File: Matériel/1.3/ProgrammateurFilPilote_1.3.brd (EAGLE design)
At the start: 85.1 x 66.7 mm, 84 parts, among them IC1 MCP23017, J2 GROVE-I2C, P1 PADSMALL, P2 PADSMALL, SW1 HLS8L-DC5V-S-C, T1 2N3904, T2 BSS138

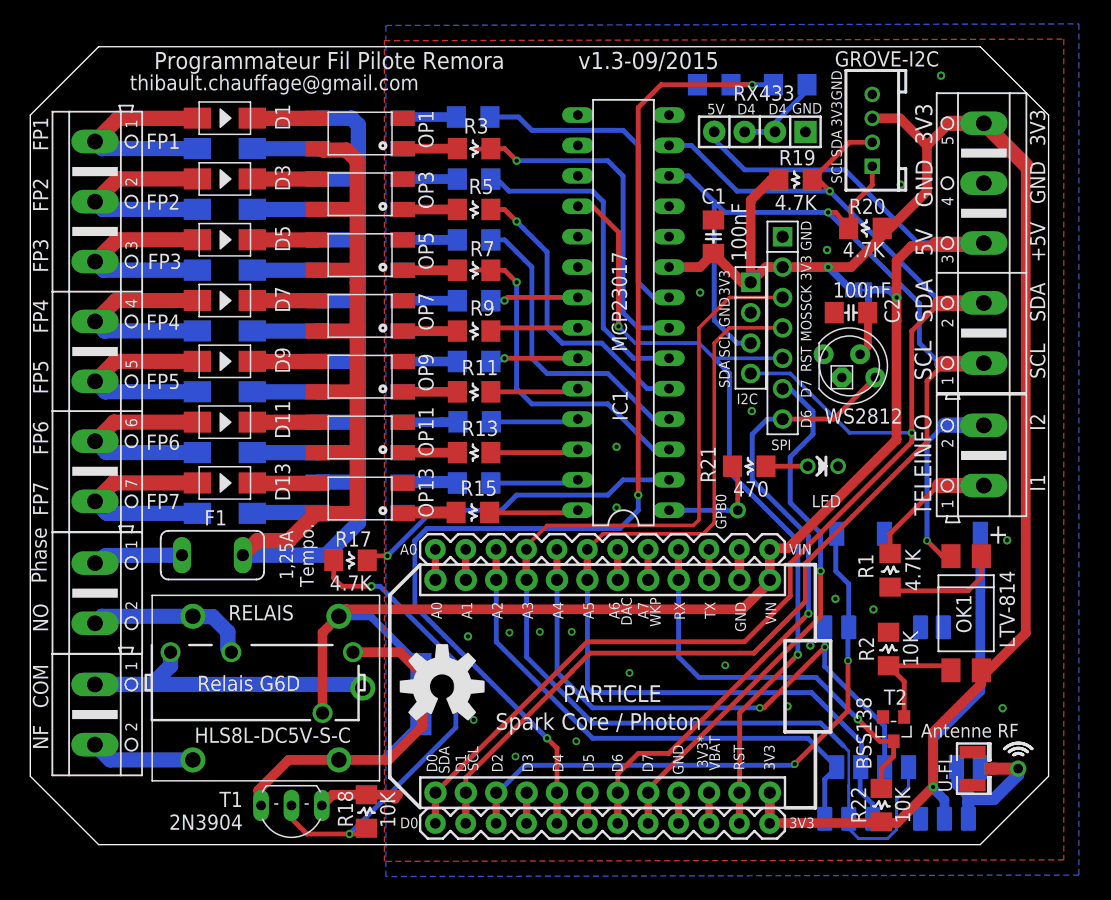
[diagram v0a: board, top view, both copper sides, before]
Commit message: Ajustements Finaux
Résistances 390 Ohm pour nouveaux optos Sharp
Commandes Opto/led via MCP par la masse
Ajustement des borniers pour boitier rail DIN
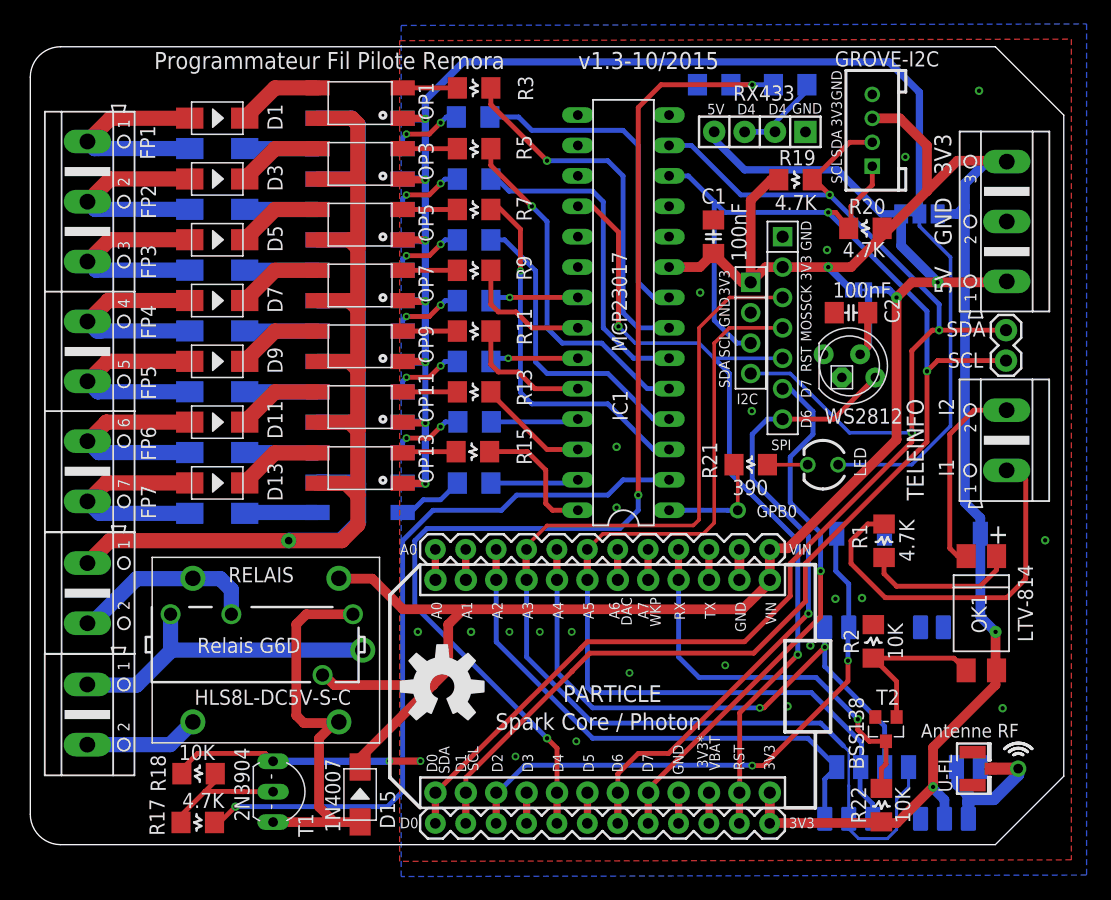
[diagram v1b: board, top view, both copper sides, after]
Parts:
- removed EXTENSION: (no value), con-ptr500:AK500/5
- removed F1: 1,25A temporisé, fuse:TE5
- added JP1: (no value), SparkFun-Connectors:1X02
- added OPTO: (no value), SparkFun-Passives:PAD-JUMPER-3-2OF3_NC_BY_TRACE_YES_SILK_LARGE
- added X1: (no value), con-ptr500:AK500/3
- LED: value (none) -> LED3MM; device _c2h:LED3MM_NOSILK -> _c2h:LED3MM
- R10, R11, R12, R13, R14, R15, R16, R21, R3, R4, R5, R6, R7, R8, R9: value 470 -> 390
- moved R17 25.4 mm to (14.0, 1.86)
- moved R18 14.4 mm to (14.1, 5.93), turned to 0 degrees
- moved D15 9.80 mm to (27.6, 4.19), flipped to the top
- moved R7 5.08 mm to (37.1, 53.1)
- moved R15 5.08 mm to (37.0, 32.8)
- moved R11 5.08 mm to (37.1, 42.9)
- moved R13 5.08 mm to (37.1, 37.8)
- moved R3 5.08 mm to (37.1, 63.2)
- moved R5 5.08 mm to (37.1, 58.2)
- moved R9 5.08 mm to (37.1, 48.0)
- moved RELAIS 3.18 mm to (18.9, 16.8)
- moved SW1 3.18 mm to (19.7, 16.3)
- moved OP5 2.54 mm to (30.7, 53.1)
- moved OP1 2.54 mm to (30.7, 63.2)
- moved OP11 2.54 mm to (30.7, 37.8)
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- renumbered SJ1 to RGB
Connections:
- removed net PHASE-SECTEUR: 230V.1, F1.1
- new net N$18: OP9.3, R11.2
- net +3V3: now also OPTO.1, X1.3; no longer EXTENSION.5
- net +5V: now also OPTO.3, X1.1; no longer EXTENSION.3
- net GND: now also X1.2; no longer EXTENSION.4, LED.MINUS, OP1.3, OP10.3, OP11.3, OP12.3, OP13.3, OP14.3, OP2.3, OP3.3, OP4.3, OP5.3, OP6.3, OP7.3, OP8.3, OP9.3
- net LED: now also R21.1; no longer R21.2
- net N$10: now also OP4.3; no longer OP4.1
- net N$11: now also OP5.3; no longer OP5.1
- net N$12: now also OP6.3; no longer OP6.1
- net N$13: now also OP7.3; no longer OP7.1
- net N$14: now also OP8.3; no longer OP8.1
- net N$19: now also LED.PLUS, OP1.1, OP10.1, OP11.1, OP12.1, OP13.1, OP14.1, OP2.1, OP3.1, OP4.1, OP5.1, OP6.1, OP7.1, OP8.1, OPTO.2; no longer R11.2
- net N$32: now also OP10.3; no longer OP10.1
- net N$34: now also OP14.3; no longer OP14.1
- net N$47: now also OP11.3; no longer OP11.1
- net N$48: now also OP12.3; no longer OP12.1
- net N$6: now also LED.MINUS, R21.2; no longer LED.PLUS, R21.1
- net N$7: now also OP1.3; no longer OP1.1
- net N$8: now also OP2.3; no longer OP2.1
- net N$9: now also OP3.3; no longer OP3.1
- net PHASE: now also 230V.1; no longer F1.2
- net S$5: now also OP13.3; no longer OP13.1
- net SCL: now also JP1.2; no longer EXTENSION.1
- net SDA: now also JP1.1; no longer EXTENSION.2
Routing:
- net N$19: track 4.57 -> 143.4 mm, vias 0 -> 7
- net RELAIS: track 29.0 -> 62.1 mm
- net N$21: track 41.1 -> 12.5 mm, vias 2 -> 0
- net N$5: track 11.2 -> 31.9 mm
- net +3V3: track 159.2 -> 138.9 mm, vias 2 -> 3
- net PHASE: track 131.2 -> 147.6 mm, vias 0 -> 1
- net GND: track 13.4 -> 26.3 mm, vias 22 -> 24
- net +5V: track 123.9 -> 131.7 mm, vias 1 -> 2
- net PHASE-SECTEUR: track 7.47 -> 0.00 mm
- net SCL: track 126.9 -> 122.1 mm, vias 1 -> 2
- net SDA: track 131.1 -> 126.5 mm, vias 2 -> 3
- net N$18: track 0.00 -> 4.57 mm
- net FP2A: track 24.8 -> 29.2 mm
- net FP3A: track 27.5 -> 31.4 mm
- net FP7A: track 7.44 -> 11.0 mm
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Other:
- board size 85.1 x 66.7 mm -> 86.4 x 66.7 mm
- board text added: "v1.3-10/2015"
- board text removed: "1,25A Tempo."
- board text removed: "Fusible"
- board text removed: "thibault.chauffage@gmail.com"
- board text removed: "v1.3-09/2015"
